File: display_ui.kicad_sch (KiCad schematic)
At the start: 68 parts, among them SW2 K2-1102SP-C4SC-04, SW3 K2-1102SP-C4SC-04, SW4 K2-1102SP-C4SC-04, SW5 K2-1102SP-C4SC-04, SW6 PEC11R-4220F-S0012, T1 AO3400A, T2 AO3400A, T3 AO3400A, T4 AO3400A, T5 AO3400A, X5 DFR0649, X9 BH-00105

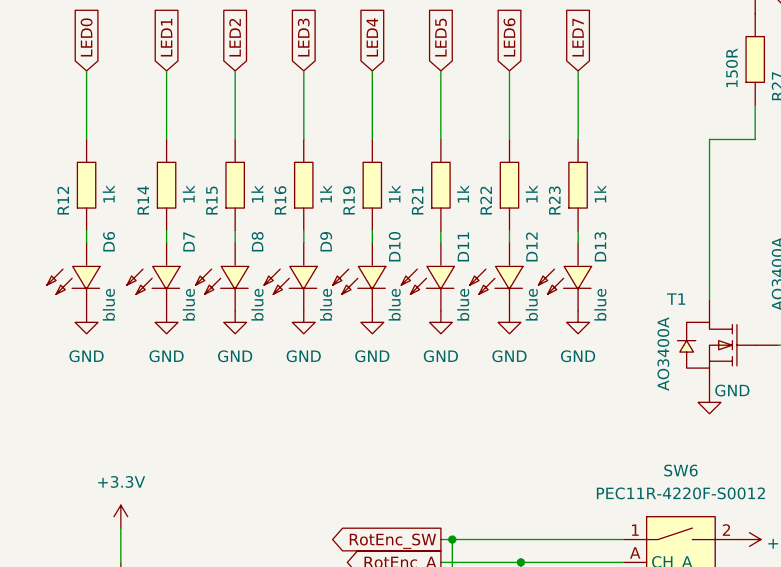
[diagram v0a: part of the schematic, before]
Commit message: fix parts (like led were wrong way round) Neatify Board
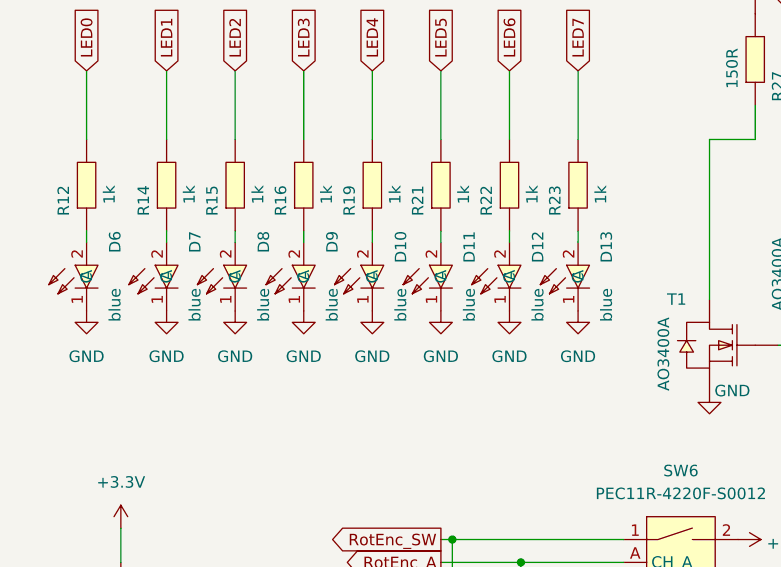
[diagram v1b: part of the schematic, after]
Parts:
- D10, D11, D12, D13, D6, D7, D8, D9: symbol eduboardv2:19-217_BHC-ZL1M2RY_3T -> EduboardV2_kicadlib:19-217_BHC-ZL1M2RY_3T; Manufacturer EVERLIGHT -> EVERLIGHT(亿光)
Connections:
- net GND: now also D10.1 (C), D11.1 (C), D12.1 (C), D13.1 (C), D6.1 (C), D7.1 (C), D8.1 (C), D9.1 (C); no longer D10.2 (C), D11.2 (C), D12.2 (C), D13.2 (C), D6.2 (C), D7.2 (C), D8.2 (C), D9.2 (C)
- net at R15.1: now also D8.2 (A); no longer D8.1 (A)
- net at R23.1: now also D13.2 (A); no longer D13.1 (A)
- net at R22.1: now also D12.2 (A); no longer D12.1 (A)
- net at R21.1: now also D11.2 (A); no longer D11.1 (A)
- net at R12.1: now also D6.2 (A); no longer D6.1 (A)
- net at R14.1: now also D7.2 (A); no longer D7.1 (A)
- net at R16.1: now also D9.2 (A); no longer D9.1 (A)
- net at R19.1: now also D10.2 (A); no longer D10.1 (A)

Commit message: ready for order first prototype
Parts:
- D14: LCSC Part Alternative (none) -> C2874116
- X9: value BH-00105 -> FH-00148; MPN (none) -> FH-00148
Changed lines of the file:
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@@
+      (effects (font (size 1.27 1.27)) hide)
+    )
+    (property "LCSC Part Alternative" "C2874116" (at 103.505 26.67 90)
       (effects (font (size 1.27 1.27)) hide)
     )
@@
       (effects (font (size 1.27 1.27)) (justify left))
     )
-    (property "Value" "BH-00105" (at 273.05 88.9 0)
+    (property "Value" "FH-00148" (at 273.05 88.9 0)
       (effects (font (size 1.27 1.27)))
     )
@@
       (effects (font (size 1.27 1.27)) hide)
     )
+    (property "MPN" "FH-00148" (at 270.51 89.535 0)
+      (effects (font (size 1.27 1.27)) hide)
+    )

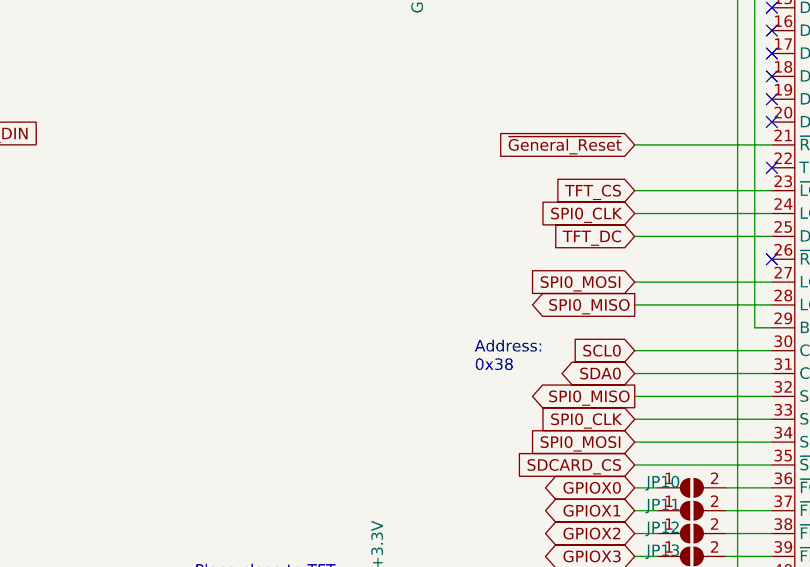
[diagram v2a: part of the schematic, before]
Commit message: mark errors found on first prototypes
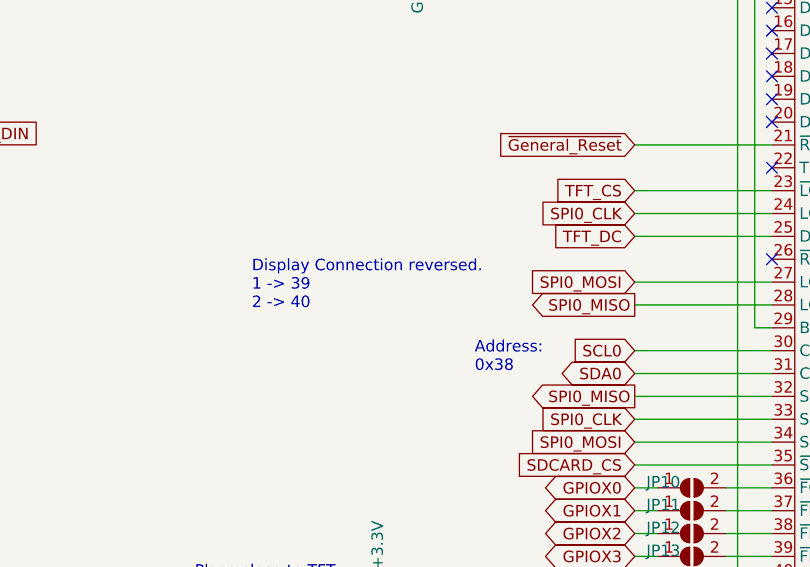
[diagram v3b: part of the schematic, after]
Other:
- note added: "Display Connection reversed. 1 -> 39 2 -> 40"
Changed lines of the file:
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@@
     (effects (font (size 1.27 1.27)) (justify left bottom))
+  )
+  (text "Display Connection reversed. \n1 -> 39\n2 -> 40" (at 199.39 113.665 0)
+    (effects (font (size 1.27 1.27) (color 251 0 0 1)) (justify left bottom))
   )
   (global_label "SDCARD_CS" (shape input) (at 241.935 130.81 180) (fields_autoplaced)

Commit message: fix some wrong jlcpcb part numbers
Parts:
- R35, R36, R37, R38: LCSC Part C25077 -> C25744
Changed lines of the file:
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@@
       (effects (font (size 1.27 1.27)) hide)
     )
-    (property "LCSC Part" "C25077" (at 95.25 107.95 0)
+    (property "LCSC Part" "C25744" (at 95.25 107.95 0)
       (effects (font (size 1.27 1.27)) hide)
     )
@@
       (effects (font (size 1.27 1.27)) hide)
     )
-    (property "LCSC Part" "C25077" (at 169.545 86.36 0)
+    (property "LCSC Part" "C25744" (at 169.545 86.36 0)
       (effects (font (size 1.27 1.27)) hide)
     )
@@
       (effects (font (size 1.27 1.27)) hide)
     )
-    (property "LCSC Part" "C25077" (at 80.01 107.95 0)
+    (property "LCSC Part" "C25744" (at 80.01 107.95 0)
       (effects (font (size 1.27 1.27)) hide)
     )
@@
       (effects (font (size 1.27 1.27)) hide)
     )
-    (property "LCSC Part" "C25077" (at 87.63 107.95 0)
+    (property "LCSC Part" "C25744" (at 87.63 107.95 0)
       (effects (font (size 1.27 1.27)) hide)
     )

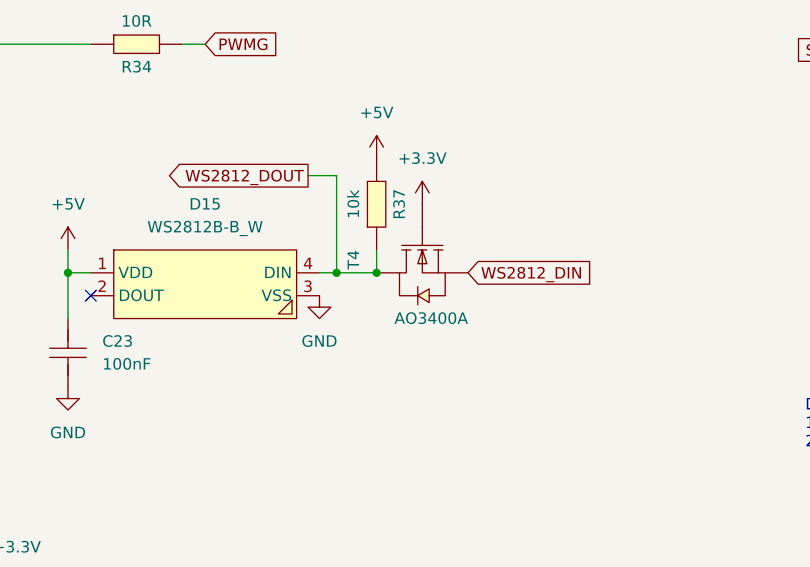
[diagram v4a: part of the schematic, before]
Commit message: change ws2812 level shifter to bsn20
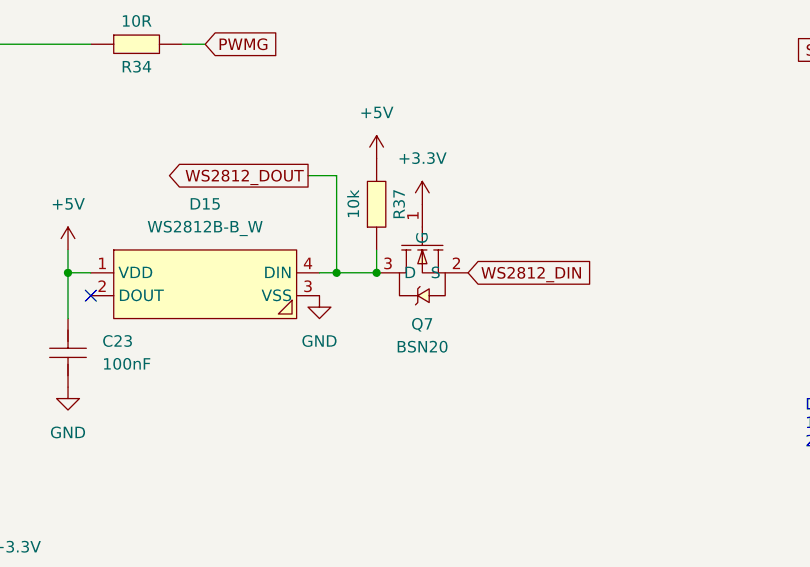
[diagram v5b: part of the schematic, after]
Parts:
- removed T4: AO3400A, EduboardV2_kicadlib:SOT-23-3_L2.9-W1.6-P1.90-LS2.8-BR, symbol eduboardv2:AO3400A
- added Q7: BSN20, EduboardV2_kicadlib:SOT-23-3_L2.9-W1.6-P1.90-LS2.8-BR, symbol EduboardV2_kicadlib:BSN20
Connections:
- net +3.3V: now also Q7.1 (G)
- net WS2812_DIN: now also Q7.2 (S)
- net WS2812_DOUT: now also Q7.3 (D)
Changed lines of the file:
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@@
   (junction (at 121.285 171.45) (diameter 0) (color 0 0 0 0)
   )
+  (junction (at 77.47 97.79) (diameter 0) (color 0 0 0 0)
+  )
+  (junction (at 81.28 167.64) (diameter 0) (color 0 0 0 0)
+  )
+  (junction (at 200.66 146.05) (diameter 0) (color 0 0 0 0)
+  )
+  (junction (at 69.85 92.71) (diameter 0) (color 0 0 0 0)
+  )
+  (junction (at 60.325 167.64) (diameter 0) (color 0 0 0 0)
+  )
   (junction (at 151.765 93.98) (diameter 0) (color 0 0 0 0)
-  )
-  (junction (at 77.47 97.79) (diameter 0) (color 0 0 0 0)
-  )
-  (junction (at 81.28 167.64) (diameter 0) (color 0 0 0 0)
-  )
-  (junction (at 200.66 146.05) (diameter 0) (color 0 0 0 0)
-  )
-  (junction (at 69.85 92.71) (diameter 0) (color 0 0 0 0)
-  )
-  (junction (at 60.325 167.64) (diameter 0) (color 0 0 0 0)
   )
   (junction (at 255.27 46.99) (diameter 0) (color 0 0 0 0)
@@
     )
   )
-  (symbol (lib_name "AO3400A_1") (lib_id "eduboardv2:AO3400A") (at 156.845 91.44 90) (mirror x) (unit 1)
-    (in_bom yes) (on_board yes) (dnp no)
-    (property "Reference" "T4" (at 149.225 91.44 0)
-      (effects (font (size 1.27 1.27)) (justify left))
-    )
-    (property "Value" "AO3400A" (at 161.925 99.06 90)
-      (effects (font (size 1.27 1.27)) (justify left))
-    )
-    (property "Footprint" "EduboardV2_kicadlib:SOT-23-3_L2.9-W1.6-P1.90-LS2.8-BR" (at 169.545 91.44 0)
-      (effects (font (size 1.27 1.27)) hide)
-    )
-    (property "Datasheet" "https://lcsc.com/product-detail/MOSFET_AOS_AO3400A_AO3400A_C20917.html" (at 174.625 91.44 0)
-      (effects (font (size 1.27 1.27)) hide)
-    )
-    (property "Manufacturer" "AOS" (at 177.165 91.44 0)
-      (effects (font (size 1.27 1.27)) hide)
-    )
-    (property "LCSC Part" "C20917" (at 179.705 91.44 0)
-      (effects (font (size 1.27 1.27)) hide)
-    )
-    (property "JLC Part" "Basic Part" (at 182.245 91.44 0)
-      (effects (font (size 1.27 1.27)) hide)
-    )
-    (property "MPN" "AO3400A" (at 167.005 91.44 0)
-      (effects (font (size 1.27 1.27)) hide)
-    )
-    (pin "1")
-    (pin "2")
-    (pin "3")
-    (instances
-      (project "EduboardV2_Baseboard"
-        (path "/280adf03-05ea-4001-ab24-a5a43e6d4cc9/92753037-c50f-47ac-9b4f-72ea899f1ef8"
-          (reference "T4") (unit 1)
-        )
-      )
-    )
-  )
   (symbol (lib_id "eduboardv2:GND") (at 20.32 180.34 0) (unit 1)
     (in_bom yes) (on_board yes) (dnp no) (fields_autoplaced)
@@
         )
       )
+    )
+  )
+  (symbol (lib_id "EduboardV2_kicadlib:BSN20") (at 156.845 91.44 90) (mirror x) (unit 1)
+    (in_bom yes) (on_board yes) (dnp no) (fields_autoplaced)
+    (property "Reference" "Q7" (at 156.845 99.695 90)
+      (effects (font (size 1.27 1.27)))
+    )
+    (property "Value" "BSN20" (at 156.845 102.235 90)
+      (effects (font (size 1.27 1.27)))
+    )
+    (property "Footprint" "EduboardV2_kicadlib:SOT-23-3_L2.9-W1.6-P1.90-LS2.8-BR" (at 169.545 91.44 0)
+      (effects (font (size 1.27 1.27)) hide)
+    )
+    (property "Datasheet" "https://lcsc.com/product-detail/MOSFET_BSN20_C116157.html" (at 172.085 91.44 0)
+      (effects (font (size 1.27 1.27)) hide)
+    )
+    (property "Manufacturer" "SHIKUES(时科)" (at 174.625 91.44 0)
+      (effects (font (size 1.27 1.27)) hide)
+    )
+    (property "LCSC Part" "C116157" (at 177.165 91.44 0)
+      (effects (font (size 1.27 1.27)) hide)
+    )
+    (property "JLC Part" "Extended Part" (at 179.705 91.44 0)
+      (effects (font (size 1.27 1.27)) hide)
+    )
+    (pin "1")
+    (pin "2")
+    (pin "3")
+    (instances
+      (project "EduboardV2_Baseboard"
+        (path "/280adf03-05ea-4001-ab24-a5a43e6d4cc9/92753037-c50f-47ac-9b4f-72ea899f1ef8"
+          (reference "Q7") (unit 1)
+        )
+      )

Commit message: add some part alternatives and create production data
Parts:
- SW6: Alternative (none) -> C143790
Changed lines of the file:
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@@
+      (effects (font (size 1.27 1.27)) hide)
+    )
+    (property "Alternative" "C143790" (at 87.63 95.25 0)
       (effects (font (size 1.27 1.27)) hide)
     )

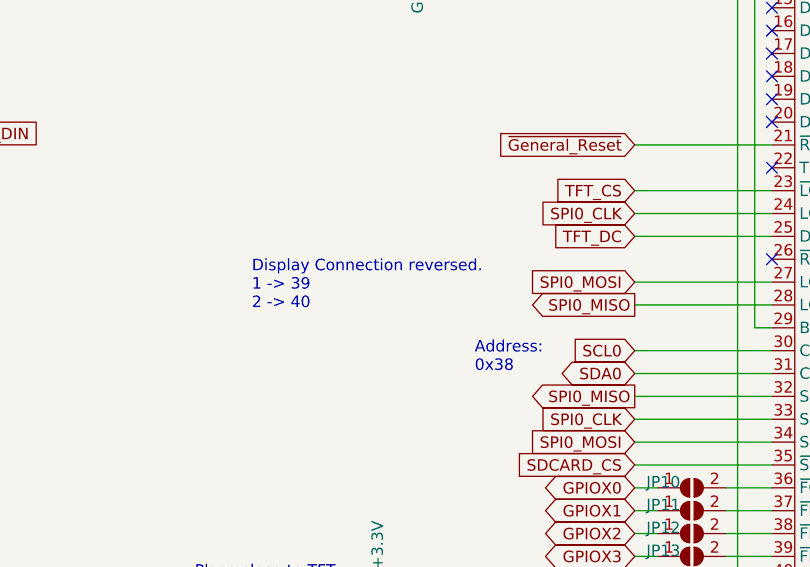
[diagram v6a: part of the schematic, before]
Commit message: Sort out RX/TX problems, improve DAC Circuits, Improve Board Text, switch out certain solder-jumpers with resistors
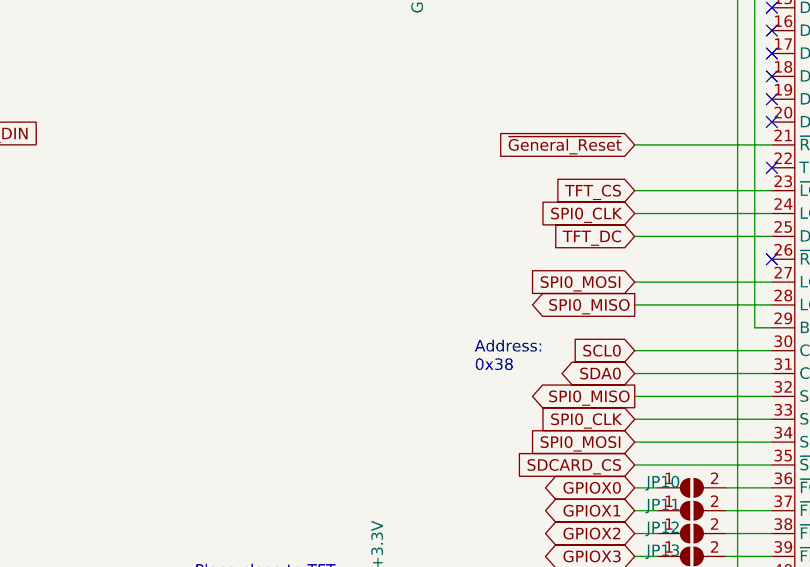
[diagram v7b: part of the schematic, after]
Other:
- note removed: "Display Connection reversed. 1 -> 39 2 -> 40"
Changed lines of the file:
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@@
     (effects (font (size 1.27 1.27)) (justify left bottom))
-  )
-  (text "Display Connection reversed. \n1 -> 39\n2 -> 40" (at 199.39 113.665 0)
-    (effects (font (size 1.27 1.27) (color 251 0 0 1)) (justify left bottom))
   )
   (global_label "SDCARD_CS" (shape input) (at 241.935 130.81 180) (fields_autoplaced)

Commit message: finalize data v2.1.
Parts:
- R13: alternative (none) -> C388854
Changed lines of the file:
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@@
+      (effects (font (size 1.27 1.27)) hide)
+    )
+    (property "alternative" "C388854" (at 25.4 97.79 90)
       (effects (font (size 1.27 1.27)) hide)
     )
